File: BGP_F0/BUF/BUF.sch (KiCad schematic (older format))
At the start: 34 parts, among them P1 CONN_01X02, P2 CONN_01X02, P3 CONN_01X03, P4 CONN_01X02, P5 CONN_01X02, P6 CONN_01X09, P7 CONN_01X03, P8 CONN_01X05, Q1 2SK208, Q2 2SK208, Q3 2SK208, Q4 2SK208, U1 MC33178

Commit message: F0 Buffer Board
Buffer done.  30mm x 40mm, with optional outboard volume or concentric vol/blend.  Output bypass EQ and straight to output possible.
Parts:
- R11, R7, R8: value 499k -> 4.99k
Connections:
- net BAT+ is gone; now on net V+: P4.1 (P1)
- net IN_B: now also C1.2, R1.1
- net IN_N: now also C2.2, R2.1
- net VRef: now also U1.1, U1.2 (-)
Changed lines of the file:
@@
 P 5200 2800
 F 0 "R7" H 5230 2820 50  0000 L CNN
-F 1 "499k" H 5230 2760 50  0000 L CNN
+F 1 "4.99k" H 5230 2760 50  0000 L CNN
 F 2 "Resistors_SMD:R_0603_HandSoldering" H 5200 2800 50  0001 C CNN
 F 3 "" H 5200 2800 50  0000 C CNN
@@
 P 5200 3200
 F 0 "R8" H 5230 3220 50  0000 L CNN
-F 1 "499k" H 5230 3160 50  0000 L CNN
+F 1 "4.99k" H 5230 3160 50  0000 L CNN
 F 2 "Resistors_SMD:R_0603_HandSoldering" H 5200 3200 50  0001 C CNN
 F 3 "" H 5200 3200 50  0000 C CNN
@@
 	0    1    1    0
 $EndComp
-Wire Wire Line
-	3800 3350 4100 3350
-Wire Wire Line
-	4100 3350 4100 2950
-Wire Wire Line
-	3200 2500 3500 2500
-Wire Wire Line
-	3350 2500 3350 2600
-Connection ~ 3350 2500
-Wire Wire Line
-	3000 2500 2800 2500
-Wire Wire Line
-	2800 2500 2800 2600
-Wire Wire Line
-	3800 2750 3800 2700
-Wire Wire Line
-	3800 2700 4250 2700
-Wire Wire Line
-	3800 4750 4100 4750
-Wire Wire Line
-	4100 4750 4100 4350
-Wire Wire Line
-	3200 3900 3500 3900
-Wire Wire Line
-	3350 3900 3350 4000
-Connection ~ 3350 3900
-Wire Wire Line
-	3000 3900 2800 3900
-Wire Wire Line
-	2800 3900 2800 4000
-Wire Wire Line
-	3800 4150 3800 4100
-Wire Wire Line
-	3800 4100 4250 4100
-Wire Wire Line
-	4450 2700 4550 2700
-Wire Wire Line
-	4450 4100 4550 4100
-Wire Wire Line
-	4550 4100 4550 3300
-Wire Wire Line
-	5000 2800 5100 2800
-Wire Wire Line
-	5000 3200 5100 3200
 $Comp
 L MC33178 U1
@@
 	1    0    0    -1
 $EndComp
-Wire Wire Line
-	5450 2800 5300 2800
-Wire Wire Line
-	5350 2800 5350 3500
-Wire Wire Line
-	5300 3200 5550 3200
-Connection ~ 5350 2800
 $Comp
 L R_Small R11
@@
 P 5650 3200
 F 0 "R11" H 5680 3220 50  0000 L CNN
-F 1 "499k" H 5680 3160 50  0000 L CNN
+F 1 "4.99k" H 5680 3160 50  0000 L CNN
 F 2 "Resistors_SMD:R_0603_HandSoldering" H 5650 3200 50  0001 C CNN
 F 3 "" H 5650 3200 50  0000 C CNN
@@
 	0    1    1    0
 $EndComp
-Connection ~ 5350 3200
-Wire Wire Line
-	5750 3200 6050 3200
-Wire Wire Line
-	6050 2700 6050 3500
 $Comp
 L Earth #PWR05
@@
 	0    1    1    0
 $EndComp
-Wire Wire Line
-	5350 3500 5550 3500
-Wire Wire Line
-	6050 3500 5750 3500
-Connection ~ 6050 3200
 $Comp
 L MC33178 U1
@@
 Text Label 5600 4150 1    60   ~ 0
 V+
-Wire Wire Line
-	5400 4550 5400 4900
-Wire Wire Line
-	5400 4900 6000 4900
-Wire Wire Line
-	6000 4900 6000 4450
 $Comp
 L R_Small R9
@@
 	1    0    0    -1
 $EndComp
-Wire Wire Line
-	5000 4750 5600 4750
-Wire Wire Line
-	5200 4750 5200 4700
-Wire Wire Line
-	5200 4150 5600 4150
-Wire Wire Line
-	5200 4350 5200 4500
-Wire Wire Line
-	5000 4350 5400 4350
 $Comp
 L CP1_Small C5
@@
 	1    0    0    -1
 $EndComp
-Wire Wire Line
-	5000 4750 5000 4700
-Connection ~ 5200 4750
-Wire Wire Line
-	5000 4500 5000 4350
-Connection ~ 5200 4350
 $Comp
 L CP1_Small C7
@@
 	0    1    1    0
 $EndComp
-Wire Wire Line
-	7250 2700 7300 2700
 Text Label 4550 2700 0    60   ~ 0
 PB1_1
@@
 	1    0    0    -1
 $EndComp
-Wire Wire Line
-	7600 3300 7600 3250
-Wire Wire Line
-	7600 3050 7600 2950
-Wire Wire Line
-	7500 2700 7600 2700
-Wire Wire Line
-	7600 2700 7600 2750
 Text Label 7600 3300 0    60   ~ 0
 PV_1
@@
 	0    -1   -1   0
 $EndComp
-Wire Wire Line
-	6050 2700 6600 2700
-Wire Wire Line
-	6600 2700 6600 2500
-Wire Wire Line
-	7050 2700 6700 2700
-Wire Wire Line
-	6700 2700 6700 2500
 $Comp
 L CONN_01X02 P1
@@
 	-1   0    0    1
 $EndComp
-Text Label 2550 2500 0    60   ~ 0
-IN_B
 Text Label 2550 3900 0    60   ~ 0
 IN_N
@@
 Text Label 8300 2850 2    60   ~ 0
 PB1_2
-Wire Wire Line
-	8300 2950 8300 3050
 Text Label 8300 3050 2    60   ~ 0
 VRef
@@
 	-1   0    0    1
 $EndComp
-Wire Wire Line
-	2550 5000 2550 4650
 Text Label 2550 5100 0    60   ~ 0
-BAT+
+V+
 Text Label 2550 4550 0    60   ~ 0
 PV_2
@@
 	1    0    0    -1
 $EndComp
+Wire Wire Line
+	3800 3350 4100 3350
+Wire Wire Line
+	4100 3350 4100 2950
+Wire Wire Line
+	3200 2500 3500 2500
+Wire Wire Line
+	3350 2500 3350 2600
+Connection ~ 3350 2500
+Wire Wire Line
+	2550 2500 3000 2500
+Wire Wire Line
+	2800 2500 2800 2600
+Wire Wire Line
+	3800 2750 3800 2700
+Wire Wire Line
+	3800 2700 4250 2700
+Wire Wire Line
+	3800 4750 4100 4750
+Wire Wire Line
+	4100 4750 4100 4350
+Wire Wire Line
+	3200 3900 3500 3900
+Wire Wire Line
+	3350 3900 3350 4000
+Connection ~ 3350 3900
+Wire Wire Line
+	2550 3900 3000 3900
+Wire Wire Line
+	2800 3900 2800 4000
+Wire Wire Line
+	3800 4150 3800 4100
+Wire Wire Line
+	3800 4100 4250 4100
+Wire Wire Line
+	4450 2700 4550 2700
+Wire Wire Line
+	4450 4100 4550 4100
+Wire Wire Line
+	4550 4100 4550 3300
+Wire Wire Line
+	5000 2800 5100 2800
+Wire Wire Line
+	5000 3200 5100 3200
+Wire Wire Line
+	5450 2800 5300 2800
+Wire Wire Line
+	5350 2800 5350 3500
+Wire Wire Line
+	5300 3200 5550 3200
+Connection ~ 5350 2800
+Connection ~ 5350 3200
+Wire Wire Line
+	5750 3200 6050 3200
+Wire Wire Line
+	6050 2700 6050 3500
+Wire Wire Line
+	5350 3500 5550 3500
+Wire Wire Line
+	6050 3500 5750 3500
+Connection ~ 6050 3200
+Wire Wire Line
+	5400 4550 5400 4900
+Wire Wire Line
+	5400 4900 6000 4900
+Wire Wire Line
+	6000 4900 6000 4450
+Wire Wire Line
+	5000 4750 5600 4750
+Wire Wire Line
+	5200 4750 5200 4700
+Wire Wire Line
+	5200 4150 5600 4150
+Wire Wire Line
+	5200 4350 5200 4500
+Wire Wire Line
+	5000 4350 5400 4350
+Wire Wire Line
+	5000 4750 5000 4700
+Connection ~ 5200 4750
+Wire Wire Line
+	5000 4500 5000 4350
+Connection ~ 5200 4350
+Wire Wire Line
+	7250 2700 7300 2700
+Wire Wire Line
+	7600 3300 7600 3250
+Wire Wire Line
+	7600 3050 7600 2950
+Wire Wire Line
+	7500 2700 7600 2700
+Wire Wire Line
+	7600 2700 7600 2750
+Wire Wire Line
+	6050 2700 6600 2700
+Wire Wire Line
+	6600 2700 6600 2500
+Wire Wire Line
+	7050 2700 6700 2700
+Wire Wire Line
+	6700 2700 6700 2500
+Wire Wire Line
+	8300 2950 8300 3050
+Wire Wire Line
+	2550 5000 2550 4650
+Text Label 2550 2500 0    60   ~ 0
+IN_B
+Connection ~ 2800 2500
+Connection ~ 2800 3900
+Text Label 6000 4450 0    60   ~ 0
+VRef
 $EndSCHEMATC

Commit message: clranup
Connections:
- net OUT_BUF is gone; now on net IN_EQ: C6.1, P5.1 (P1), P8.2 (P2), R11.1, U1.7
- net IN_B: now also C2.2, P2.2 (P2), R2.1; no longer C1.2, P1.2 (P2), R1.1
- net IN_EQ: no longer P5.2 (P2), P8.1 (P1), R12.2
- net IN_N: now also C1.2, P1.2 (P2), R1.1; no longer C2.2, P2.2 (P2), R2.1
- new net OUT_EQ: P5.2 (P2), P8.1 (P1), R12.2
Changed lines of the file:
@@
 PV_3
 Text Label 7050 2700 2    60   ~ 0
+OUT_EQ
+Text Label 6350 2700 0    60   ~ 0
 IN_EQ
-Text Label 6050 2700 0    60   ~ 0
-OUT_BUF
 $Comp
 L CONN_01X02 P5
@@
 $EndComp
 Text Label 2550 3900 0    60   ~ 0
-IN_N
+IN_B
 $Comp
 L CONN_01X09 P6
@@
 VRef
 Text Label 8300 3900 2    60   ~ 0
-OUT_BUF
+IN_EQ
 Text Label 8300 3800 2    60   ~ 0
-IN_EQ
+OUT_EQ
 Text Label 8300 4000 2    60   ~ 0
 V+
@@
 	2550 5000 2550 4650
 Text Label 2550 2500 0    60   ~ 0
-IN_B
+IN_N
 Connection ~ 2800 2500
 Connection ~ 2800 3900

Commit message: F0 BUF is now 26x40
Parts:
- Q1, Q2, Q3, Q4: footprint TO_SOT_Packages_SMD:SOT-323_SC-70_Handsoldering -> TO_SOT_Packages_SMD:SC-59
- R1, R10, R11, R12, R13, R14, R2, R3, R4, R5, R6, R7, R8, R9: footprint Resistors_SMD:R_0603_HandSoldering -> Resistors_SMD:R_0603
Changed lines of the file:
@@
 F 0 "R1" H 2830 2720 50  0000 L CNN
 F 1 "499k" H 2830 2660 50  0000 L CNN
-F 2 "Resistors_SMD:R_0603_HandSoldering" H 2800 2700 50  0001 C CNN
+F 2 "Resistors_SMD:R_0603" H 2800 2700 50  0001 C CNN
 F 3 "" H 2800 2700 50  0000 C CNN
 	1    2800 2700
@@
 F 0 "R3" H 3380 2720 50  0000 L CNN
 F 1 "499k" H 3380 2660 50  0000 L CNN
-F 2 "Resistors_SMD:R_0603_HandSoldering" H 3350 2700 50  0001 C CNN
+F 2 "Resistors_SMD:R_0603" H 3350 2700 50  0001 C CNN
 F 3 "" H 3350 2700 50  0000 C CNN
 	1    3350 2700
@@
 F 0 "Q1" H 4000 2550 50  0000 R CNN
 F 1 "2SK208" H 4200 2450 50  0000 R CNN
-F 2 "TO_SOT_Packages_SMD:SOT-323_SC-70_Handsoldering" H 3900 2600 50  0001 C CNN
+F 2 "TO_SOT_Packages_SMD:SC-59" H 3900 2600 50  0001 C CNN
 F 3 "" H 3700 2500 50  0000 C CNN
 	1    3700 2500
@@
 F 0 "Q3" H 4200 3000 50  0000 R CNN
 F 1 "2SK208" H 4400 2900 50  0000 R CNN
-F 2 "TO_SOT_Packages_SMD:SOT-323_SC-70_Handsoldering" H 4100 3050 50  0001 C CNN
+F 2 "TO_SOT_Packages_SMD:SC-59" H 4100 3050 50  0001 C CNN
 F 3 "" H 3900 2950 50  0000 C CNN
 	1    3900 2950
@@
 F 0 "R5" H 3830 3270 50  0000 L CNN
 F 1 "20k" H 3830 3210 50  0000 L CNN
-F 2 "Resistors_SMD:R_0603_HandSoldering" H 3800 3250 50  0001 C CNN
+F 2 "Resistors_SMD:R_0603" H 3800 3250 50  0001 C CNN
 F 3 "" H 3800 3250 50  0000 C CNN
 	1    3800 3250
@@
 F 0 "R2" H 2830 4120 50  0000 L CNN
 F 1 "499k" H 2830 4060 50  0000 L CNN
-F 2 "Resistors_SMD:R_0603_HandSoldering" H 2800 4100 50  0001 C CNN
+F 2 "Resistors_SMD:R_0603" H 2800 4100 50  0001 C CNN
 F 3 "" H 2800 4100 50  0000 C CNN
 	1    2800 4100
@@
 F 0 "R4" H 3380 4120 50  0000 L CNN
 F 1 "499k" H 3380 4060 50  0000 L CNN
-F 2 "Resistors_SMD:R_0603_HandSoldering" H 3350 4100 50  0001 C CNN
+F 2 "Resistors_SMD:R_0603" H 3350 4100 50  0001 C CNN
 F 3 "" H 3350 4100 50  0000 C CNN
 	1    3350 4100
@@
 F 0 "Q2" H 4000 3950 50  0000 R CNN
 F 1 "2SK208" H 4200 3850 50  0000 R CNN
-F 2 "TO_SOT_Packages_SMD:SOT-323_SC-70_Handsoldering" H 3900 4000 50  0001 C CNN
+F 2 "TO_SOT_Packages_SMD:SC-59" H 3900 4000 50  0001 C CNN
 F 3 "" H 3700 3900 50  0000 C CNN
 	1    3700 3900
@@
 F 0 "Q4" H 4200 4400 50  0000 R CNN
 F 1 "2SK208" H 4400 4300 50  0000 R CNN
-F 2 "TO_SOT_Packages_SMD:SOT-323_SC-70_Handsoldering" H 4100 4450 50  0001 C CNN
+F 2 "TO_SOT_Packages_SMD:SC-59" H 4100 4450 50  0001 C CNN
 F 3 "" H 3900 4350 50  0000 C CNN
 	1    3900 4350
@@
 F 0 "R6" H 3830 4670 50  0000 L CNN
 F 1 "20k" H 3830 4610 50  0000 L CNN
-F 2 "Resistors_SMD:R_0603_HandSoldering" H 3800 4650 50  0001 C CNN
+F 2 "Resistors_SMD:R_0603" H 3800 4650 50  0001 C CNN
 F 3 "" H 3800 4650 50  0000 C CNN
 	1    3800 4650
@@
 F 0 "R7" H 5230 2820 50  0000 L CNN
 F 1 "4.99k" H 5230 2760 50  0000 L CNN
-F 2 "Resistors_SMD:R_0603_HandSoldering" H 5200 2800 50  0001 C CNN
+F 2 "Resistors_SMD:R_0603" H 5200 2800 50  0001 C CNN
 F 3 "" H 5200 2800 50  0000 C CNN
 	1    5200 2800
@@
 F 0 "R8" H 5230 3220 50  0000 L CNN
 F 1 "4.99k" H 5230 3160 50  0000 L CNN
-F 2 "Resistors_SMD:R_0603_HandSoldering" H 5200 3200 50  0001 C CNN
+F 2 "Resistors_SMD:R_0603" H 5200 3200 50  0001 C CNN
 F 3 "" H 5200 3200 50  0000 C CNN
 	1    5200 3200
@@
 F 0 "R11" H 5680 3220 50  0000 L CNN
 F 1 "4.99k" H 5680 3160 50  0000 L CNN
-F 2 "Resistors_SMD:R_0603_HandSoldering" H 5650 3200 50  0001 C CNN
+F 2 "Resistors_SMD:R_0603" H 5650 3200 50  0001 C CNN
 F 3 "" H 5650 3200 50  0000 C CNN
 	1    5650 3200
@@
 F 0 "R9" H 5230 4270 50  0000 L CNN
 F 1 "100k" H 5230 4210 50  0000 L CNN
-F 2 "Resistors_SMD:R_0603_HandSoldering" H 5200 4250 50  0001 C CNN
+F 2 "Resistors_SMD:R_0603" H 5200 4250 50  0001 C CNN
 F 3 "" H 5200 4250 50  0000 C CNN
 	1    5200 4250
@@
 F 0 "R10" H 5230 4620 50  0000 L CNN
 F 1 "100k" H 5230 4560 50  0000 L CNN
-F 2 "Resistors_SMD:R_0603_HandSoldering" H 5200 4600 50  0001 C CNN
+F 2 "Resistors_SMD:R_0603" H 5200 4600 50  0001 C CNN
 F 3 "" H 5200 4600 50  0000 C CNN
 	1    5200 4600
@@
 F 0 "R12" H 7180 2720 50  0000 L CNN
 F 1 "100" H 7180 2660 50  0000 L CNN
-F 2 "Resistors_SMD:R_0603_HandSoldering" H 7150 2700 50  0001 C CNN
+F 2 "Resistors_SMD:R_0603" H 7150 2700 50  0001 C CNN
 F 3 "" H 7150 2700 50  0000 C CNN
 	1    7150 2700
@@
 F 0 "R13" H 7630 2870 50  0000 L CNN
 F 1 "10k" H 7630 2810 50  0000 L CNN
-F 2 "Resistors_SMD:R_0603_HandSoldering" H 7600 2850 50  0001 C CNN
+F 2 "Resistors_SMD:R_0603" H 7600 2850 50  0001 C CNN
 F 3 "" H 7600 2850 50  0000 C CNN
 	1    7600 2850
@@
 F 0 "R14" H 7630 3170 50  0000 L CNN
 F 1 "12k" H 7630 3110 50  0000 L CNN
-F 2 "Resistors_SMD:R_0603_HandSoldering" H 7600 3150 50  0001 C CNN
+F 2 "Resistors_SMD:R_0603" H 7600 3150 50  0001 C CNN
 F 3 "" H 7600 3150 50  0000 C CNN
 	1    7600 3150

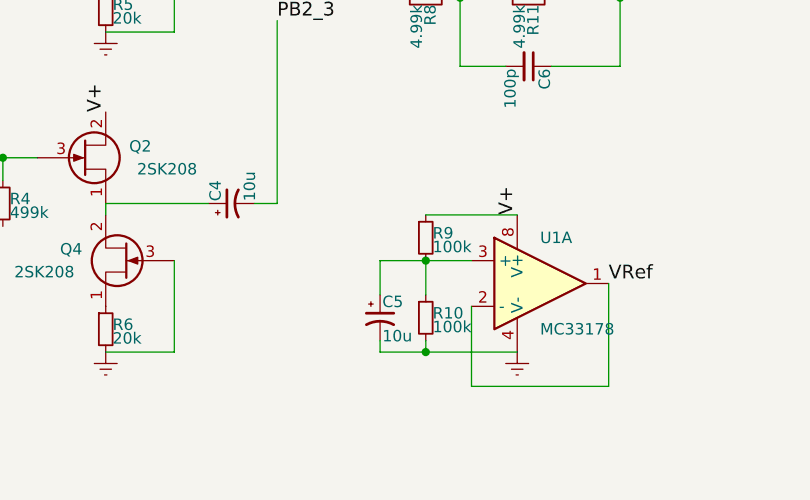
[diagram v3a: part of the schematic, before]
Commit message: F0 prot diode added, bt changed to 26mm
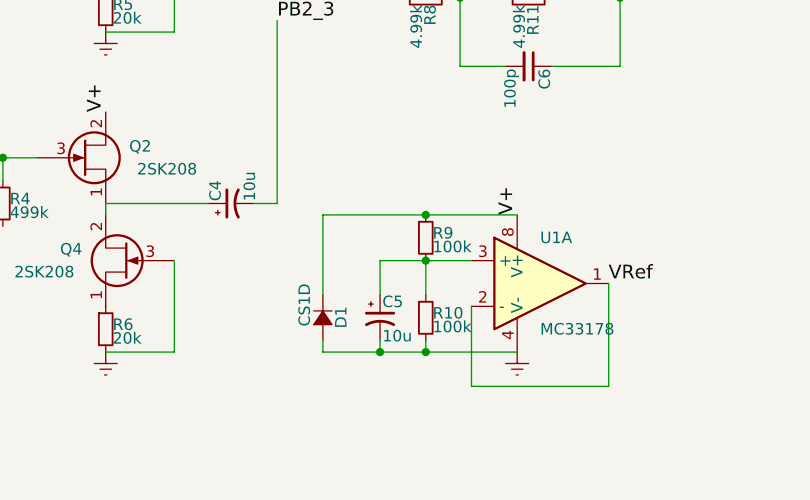
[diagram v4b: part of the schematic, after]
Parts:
- added D1: CS1D, Diodes_SMD:D_SMA, symbol D_Small_ALT
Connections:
- net Earth: now also D1.2 (A)
- net V+: now also D1.1 (K)
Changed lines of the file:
@@
 	6000 4900 6000 4450
 Wire Wire Line
-	5000 4750 5600 4750
+	4750 4750 5600 4750
 Wire Wire Line
 	5200 4750 5200 4700
 Wire Wire Line
-	5200 4150 5600 4150
+	4750 4150 5600 4150
 Wire Wire Line
 	5200 4350 5200 4500
@@
 Text Label 6000 4450 0    60   ~ 0
 VRef
+$Comp
+L D_Small_ALT D1
+U 1 1 5A68E289
+P 4750 4600
+F 0 "D1" H 4700 4680 50  0000 L CNN
+F 1 "CS1D" H 4600 4520 50  0000 L CNN
+F 2 "Diodes_SMD:D_SMA" V 4750 4600 50  0001 C CNN
+F 3 "" V 4750 4600 50  0001 C CNN
+	1    4750 4600
+	0    1    1    0
+$EndComp
+Wire Wire Line
+	4750 4500 4750 4150
+Connection ~ 5200 4150
+Wire Wire Line
+	4750 4700 4750 4750
+Connection ~ 5000 4750
 $EndSCHEMATC

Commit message: Some Changes
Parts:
- removed Q3, Q4: 2SK208, TO_SOT_Packages_SMD:SC-59, symbol Q_NJFET_SDG
- removed R5, R6: 20k, Resistors_SMD:R_0603, symbol R_Small
- added C8, C9: 27p, Capacitors_SMD:C_0603_HandSoldering, symbol C_Small
- added D2, D3: S-301, Diodes_SMD:SOD-123, symbol D_Small
- Q1, Q2: value 2SK208 -> 2N5457
- R1, R2: value 499k -> 1.5MEG
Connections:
- wire segments 51 -> 49
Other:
- moved on the sheet: C1, C2, P1, P2, P3, P4, R1, R2, R3, R4

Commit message: F0 Final
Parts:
- removed C1, C2: 0.1u, Capacitors_SMD:C_1206_HandSoldering, symbol C_Small
- removed C8, C9: 27p, Capacitors_SMD:C_0603_HandSoldering, symbol C_Small
- removed D2, D3: S-301, Diodes_SMD:SOD-123, symbol D_Small
- removed P5: CONN_01X02, Connectors_JST:JST_PH_B2B-PH-K_02x2.00mm_Straight, symbol CONN_01X02
- removed P7: CONN_01X03, Connectors_JST:JST_PH_B3B-PH-K_03x2.00mm_Straight, symbol CONN_01X03
- added C1, C2: 0.1u, Capacitors_Tantalum_SMD:TantalC_SizeR_EIA-2012, symbol CP1_Small
- added P7: CONN_01X02, Connectors_JST:JST_PH_B2B-PH-K_02x2.00mm_Straight, symbol CONN_01X02
- added R13, R14: 20k, Resistors_SMD:R_0603, symbol R_Small
- added R15, R16: 1k, Resistors_SMD:R_0603, symbol R_Small
- C3, C4: value 10u -> 1u; footprint Capacitors_SMD:C_0805_HandSoldering -> Capacitors_Tantalum_SMD:TantalC_SizeR_EIA-2012
- C5, C7: footprint Capacitors_SMD:C_0805_HandSoldering -> Capacitors_Tantalum_SMD:TantalC_SizeR_EIA-2012
- C6: footprint Capacitors_SMD:C_0805_HandSoldering -> Capacitors_SMD:C_0805
- R1, R2: value 1.5MEG -> 330k
- R3, R4: value 499k -> 1MEG
- R9: renamed from R11; value 4.99k -> 10k
- renumbered D1 to D3, P6 to P5, P8 to P6, R12 to R10, R13 to R11, R14 to R12, R7 to R5, R8 to R6, R9 to R7, R10 to R8
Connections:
- wire segments 49 -> 47
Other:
- moved on the sheet: P1, P2, P3, P4, R1, R2, R3, R4

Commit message: F0 Final
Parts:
- C6: footprint Capacitors_SMD:C_0805 -> Capacitors_SMD:C_0603
- R5, R6: value 4.99k -> 49.9k
- R9: value 10k -> 100k
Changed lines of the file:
@@
 P 5200 2800
 F 0 "R5" H 5230 2820 50  0000 L CNN
-F 1 "4.99k" H 5230 2760 50  0000 L CNN
+F 1 "49.9k" H 5230 2760 50  0000 L CNN
 F 2 "Resistors_SMD:R_0603" H 5200 2800 50  0001 C CNN
 F 3 "" H 5200 2800 50  0000 C CNN
@@
 P 5200 3200
 F 0 "R6" H 5230 3220 50  0000 L CNN
-F 1 "4.99k" H 5230 3160 50  0000 L CNN
+F 1 "49.9k" H 5230 3160 50  0000 L CNN
 F 2 "Resistors_SMD:R_0603" H 5200 3200 50  0001 C CNN
 F 3 "" H 5200 3200 50  0000 C CNN
@@
 P 5650 3200
 F 0 "R9" H 5680 3220 50  0000 L CNN
-F 1 "10k" H 5680 3160 50  0000 L CNN
+F 1 "100k" H 5680 3160 50  0000 L CNN
 F 2 "Resistors_SMD:R_0603" H 5650 3200 50  0001 C CNN
 F 3 "" H 5650 3200 50  0000 C CNN
@@
 F 0 "C6" H 5660 3570 50  0000 L CNN
 F 1 "100p" H 5660 3420 50  0000 L CNN
-F 2 "Capacitors_SMD:C_0805" H 5650 3500 50  0001 C CNN
+F 2 "Capacitors_SMD:C_0603" H 5650 3500 50  0001 C CNN
 F 3 "" H 5650 3500 50  0000 C CNN
 	1    5650 3500

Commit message: Some fixes and refinement
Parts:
- added R17: 10k, Resistors_SMD:R_0603, symbol R_Small
- R9: value 100k -> 15k
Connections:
- wire segments 47 -> 52
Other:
- moved on the sheet: C5, C6, C7, D3, P5, P6, P7, R10, R11, R12, R7, R8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
